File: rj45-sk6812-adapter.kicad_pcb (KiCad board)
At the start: 2 copper layers, 30.5 x 44.5 mm, 10 parts, among them J1 RJ45, J2 Barrel_Jack, J3 USB_B_Mini, J4 Conn_01x08, J5 Conn_01x03, J6 Conn_01x03, J7 Conn_01x03, J8 Conn_01x03

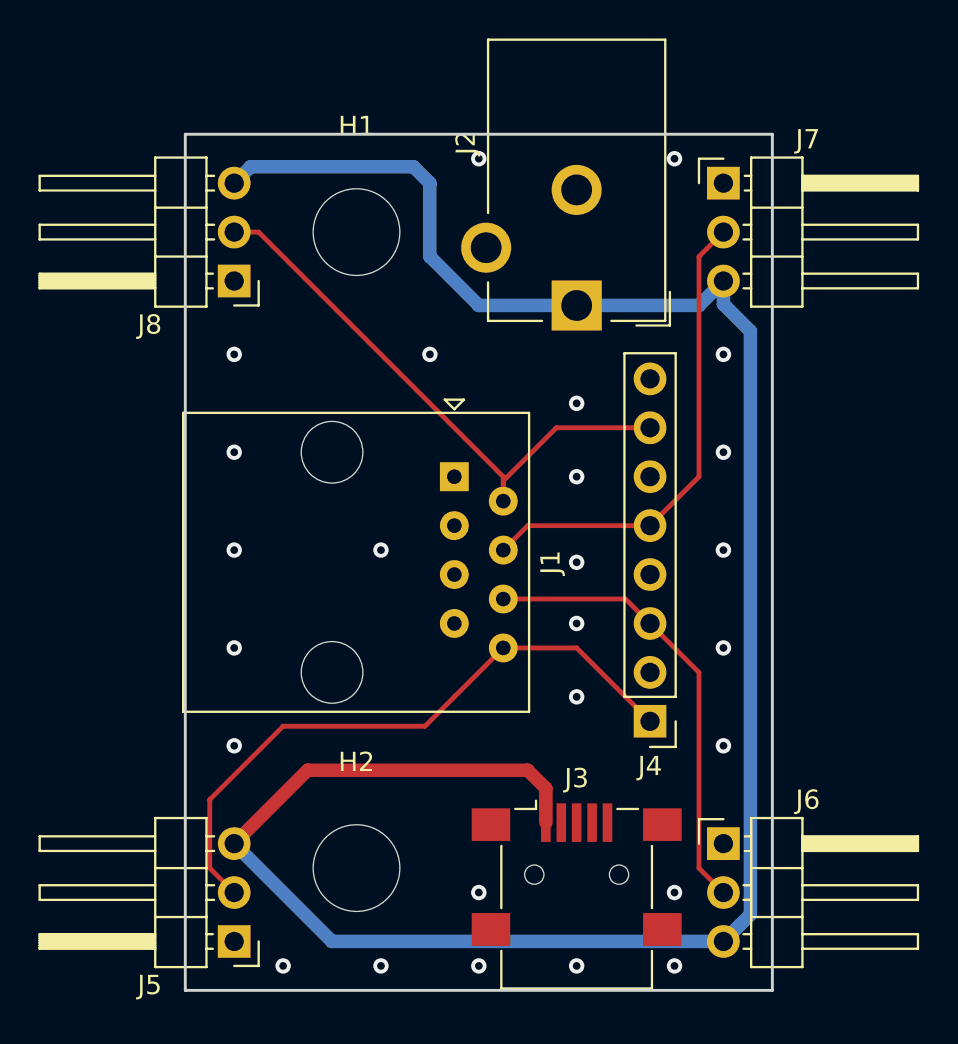
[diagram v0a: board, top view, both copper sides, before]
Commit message: Finished layouting
Added an optional circuit to blink an LED during data transmission
and a diode protected and 5V regulated power supply connector.
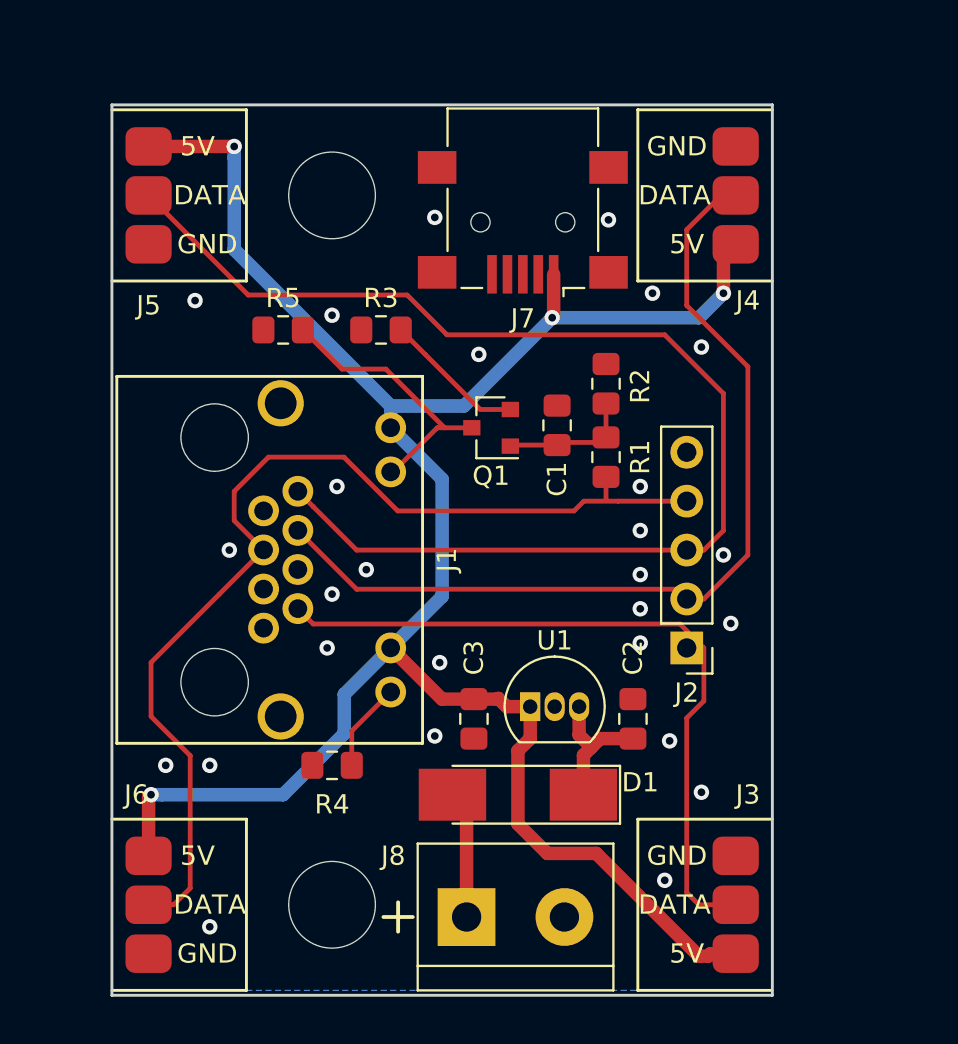
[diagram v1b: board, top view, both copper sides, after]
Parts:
- added C1: 1nF, Capacitor_SMD:C_0805_2012Metric_Pad1.15x1.40mm_HandSolder, F.Cu at (150.1, 73.5)
- added C2: 22uF, Capacitor_SMD:C_0805_2012Metric_Pad1.15x1.40mm_HandSolder, F.Cu at (154.1, 88.8)
- added C3: 22uF, Capacitor_SMD:C_0805_2012Metric_Pad1.15x1.40mm_HandSolder, F.Cu at (145.8, 88.8)
- added D1: D, Diode_SMD:D_MELF_Handsoldering, F.Cu at (148.1, 92.7)
- added Q1: 2N7002, Package_TO_SOT_SMD:SOT-23, F.Cu at (146.7, 73.7)
- added R1: 20k, Resistor_SMD:R_0805_2012Metric_Pad1.15x1.40mm_HandSolder, F.Cu at (152.7, 75.2)
- added R2: 10k, Resistor_SMD:R_0805_2012Metric_Pad1.15x1.40mm_HandSolder, F.Cu at (152.7, 71.4)
- added R3: 470R, Resistor_SMD:R_0805_2012Metric_Pad1.15x1.40mm_HandSolder, F.Cu at (141.0, 68.6)
- added R4: 470R, Resistor_SMD:R_0805_2012Metric_Pad1.15x1.40mm_HandSolder, F.Cu at (138.4, 91.2)
- added R5: 470R, Resistor_SMD:R_0805_2012Metric_Pad1.15x1.40mm_HandSolder, F.Cu at (135.9, 68.6)
- added U1: L78L05_TO92, Package_TO_SOT_THT:TO-92_Inline, F.Cu at (148.7, 88.1)
- J1: value RJ45 -> TE-Connectivity-406549-6; footprint Connector_RJ:RJ45_Amphenol_54602-x08_Horizontal -> Matthias:TE-Connectivity-406549-6
- J2: value Barrel_Jack -> Conn_01x05; footprint Connector_BarrelJack:BarrelJack_CUI_PJ-102AH_Horizontal -> Connector_PinHeader_2.54mm:PinHeader_1x05_P2.54mm_Vertical
- J3: value USB_B_Mini -> Conn_01x03; footprint Connector_USB:USB_Mini-B_Lumberg_2486_01_Horizontal -> Matthias:WS6812-SK6812
- J4: value Conn_01x08 -> Conn_01x03; footprint Connector_PinHeader_2.54mm:PinHeader_1x08_P2.54mm_Vertical -> Matthias:WS6812-SK6812
- J5, J6: footprint Connector_PinHeader_2.54mm:PinHeader_1x03_P2.54mm_Horizontal -> Matthias:WS6812-SK6812
- J7: value Conn_01x03 -> USB_B_Mini; footprint Connector_PinHeader_2.54mm:PinHeader_1x03_P2.54mm_Horizontal -> Connector_USB:USB_Mini-B_Lumberg_2486_01_Horizontal
- J8: value Conn_01x03 -> Screw_Terminal_01x02; footprint Connector_PinHeader_2.54mm:PinHeader_1x03_P2.54mm_Horizontal -> TerminalBlock:TerminalBlock_bornier-2_P5.08mm
- moved J5 39.0 mm to (128.9, 61.6), turned to 270 degrees
- moved J8 35.2 mm to (145.4, 99.1), turned to 0 degrees
- moved J6 30.0 mm to (128.9, 98.4), turned to 270 degrees
- moved J4 27.7 mm to (159.4, 61.6), turned to 90 degrees
- moved J2 18.7 mm to (156.8, 85.1)
- moved J1 13.2 mm to (132.3, 80.5)
- moved J7 10.6 mm to (148.3, 63.0), turned to 180 degrees
- moved J3 8.40 mm to (159.4, 98.4), turned to 90 degrees
- moved H1 2.29 mm to (138.4, 61.6)
- moved H2 2.29 mm to (138.4, 98.4)
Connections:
- J1 pad 2: /DATA4 -> /DATA1
- J1 pad 4: /DATA3 -> GND
- J1 pad 5: GND -> /DATA4
- J1 pad 8: /DATA1 -> /DATA3
- J2 pad 1: +5V -> /DATA1
- J2 pad 2: GND -> /DATA2
- J2 pad 3: (no net) -> /DATA3
- J3 pad 2: (no net) -> /DATA1
- J3 pad 3: (no net) -> GND
- J4 pad 1: /DATA1 -> +5V
- J4 pad 2: GND -> /DATA2
- J4 pad 3: /DATA2 -> GND
- J5 pad 1: GND -> +5V
- J5 pad 2: /DATA1 -> /DATA3
- J5 pad 3: +5V -> GND
- J6 pad 1: GND -> +5V
- J6 pad 2: /DATA2 -> /DATA4
- J6 pad 3: +5V -> GND
- J7 pad 1: GND -> +5V
- J7 pad 2: /DATA3 -> Net-(J7-Pad2)
- J7 pad 3: +5V -> Net-(J7-Pad3)
- J8 pad 1: GND -> Net-(D1-Pad2)
- J8 pad 2: /DATA4 -> GND
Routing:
- net /DATA3: track 25.0 -> 65.0 mm
- net /DATA2: track 23.7 -> 47.3 mm
- net /DATA4: track 30.3 -> 53.8 mm
- net Net-(J1-Pad11): track 0.00 -> 14.5 mm
- net Net-(Q1-Pad2): track 0.00 -> 7.64 mm
- net VDC: track 0.00 -> 7.35 mm
- net Net-(D1-Pad2): track 0.00 -> 6.65 mm
- net Net-(C1-Pad1): track 0.00 -> 6.36 mm
- net /DATA1: track 33.1 -> 37.8 mm
- net Net-(J1-Pad9): track 0.00 -> 4.64 mm
- net +5V: track 114.4 -> 110.0 mm, vias 0 -> 4
- net GND: vias 26 -> 27
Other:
- board size 30.5 x 44.5 mm -> 34.3 x 46.2 mm
